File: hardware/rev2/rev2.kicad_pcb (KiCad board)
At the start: 2 copper layers, 24 parts, among them J1 Conn_01x09_Female, J2 RFM9X_header, J3 Conn_02x03_Odd_Even, U2 MPL3115A2, U3 Teensy3.6, U5 ADXL345BCCZ, U7 TPS2113ADRBR

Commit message: wip
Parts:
- moved VDD1 17.0 mm to (163.1, 131.8)
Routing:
- net 3.3V_TEENSY: track 9.55 -> 37.8 mm, vias 0 -> 2
- net Net-(C9-Pad1): track 11.3 -> 16.5 mm, vias 0 -> 1
- net GND: track 42.1 -> 46.1 mm, vias 4 -> 5
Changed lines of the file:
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@@
     (thickness 1.6)
     (drawings 18)
-    (tracks 147)
+    (tracks 172)
     (zones 0)
     (modules 24)
@@
   )
   (setup
-    (last_trace_width 0.55)
+    (last_trace_width 1)
     (user_trace_width 0.475)
     (user_trace_width 0.55)
@@
   )
   (module footprints:Test-Point-Pin_Drill2.79mm (layer F.Cu)
-    (at 178.943 137.795 180)
+    (at 163.068 131.7752 180)
     (fp_text reference VDD1 (at 0 3.98) (layer F.SilkS)
       (effects (font (size 1 1) (thickness 0.15)))
@@
   (segment (start 161.5821 113.8903) (end 157.6451 113.8903) (width 1) (layer F.Cu) (net 1) (status C00030))
   (segment (start 157.6451 113.8903) (end 153.7081 113.8903) (width 1) (layer F.Cu) (net 1) (status C00030))
-  (segment (start 163.6549 109.4179) (end 163.6549 111.0461) (width 1) (layer F.Cu) (net 1) (status 400010))
-  (segment (start 163.6395 113.8809) (end 163.6268 113.8936) (width 1) (layer B.Cu) (net 1))
-  (segment (start 163.6395 111.0615) (end 163.6395 113.8809) (width 1) (layer B.Cu) (net 1))
-  (via (at 163.6268 113.8936) (size 1.2) (drill 0.6) (layers F.Cu B.Cu) (net 1))
-  (segment (start 163.6108 113.8776) (end 163.6268 113.8936) (width 1) (layer F.Cu) (net 1))
-  (segment (start 163.6108 113.8776) (end 161.5821 113.8903) (width 1) (layer F.Cu) (net 1) (status 800010))
-  (via (at 163.6395 111.0615) (size 1.2) (drill 0.6) (layers F.Cu B.Cu) (net 1))
-  (segment (start 163.6549 111.0461) (end 163.6395 111.0615) (width 1) (layer F.Cu) (net 1))
   (segment (start 144.9545 110.5695) (end 144.78 110.744) (width 1) (layer F.Cu) (net 1))
   (segment (start 144.78 110.744) (end 144.9705 110.5535) (width 1) (layer F.Cu) (net 1))
@@
   (segment (start 150.622 108.8136) (end 151.5364 109.728) (width 1) (layer B.Cu) (net 1))
   (segment (start 151.5364 109.728) (end 151.5364 113.8936) (width 1) (layer B.Cu) (net 1))
-  (segment (start 161.5821 112.2553) (end 167.1701 112.2553) (width 0.25) (layer F.Cu) (net 2) (status 10))
-  (segment (start 169.5196 112.2553) (end 169.9006 112.6363) (width 0.25) (layer F.Cu) (net 2) (status C00030))
-  (segment (start 167.1701 112.2553) (end 169.5196 112.2553) (width 0.25) (layer F.Cu) (net 2) (status 800020))
+  (segment (start 139.7 110.76) (end 139.7 109.8804) (width 1) (layer F.Cu) (net 1) (status 400000))
+  (via (at 143.6116 108.9152) (size 0.8) (drill 0.4) (layers F.Cu B.Cu) (net 1))
+  (segment (start 142.1384 108.9152) (end 143.6116 108.9152) (width 1) (layer F.Cu) (net 1))
+  (via (at 142.1384 108.9152) (size 0.8) (drill 0.4) (layers F.Cu B.Cu) (net 1))
+  (segment (start 140.6652 108.9152) (end 142.1384 108.9152) (width 1) (layer B.Cu) (net 1))
+  (via (at 140.6652 108.9152) (size 0.8) (drill 0.4) (layers F.Cu B.Cu) (net 1))
+  (segment (start 139.7 109.8804) (end 140.6652 108.9152) (width 1) (layer F.Cu) (net 1))
+  (segment (start 163.6549 109.4179) (end 163.6549 111.8175) (width 0.55) (layer F.Cu) (net 1) (status 400000))
+  (segment (start 163.6549 111.8175) (end 161.5821 113.8903) (width 0.55) (layer F.Cu) (net 1) (status 800000))
   (segment (start 162.4049 109.4179) (end 162.4049 111.0675) (width 0.25) (layer F.Cu) (net 2) (status 400000))
   (segment (start 162.4049 111.0675) (end 161.5821 111.8903) (width 0.25) (layer F.Cu) (net 2) (status 800000))
+  (segment (start 161.5821 111.8903) (end 160.4993 111.8903) (width 0.25) (layer F.Cu) (net 2) (status 400000))
+  (segment (start 168.5417 113.9952) (end 169.9006 112.6363) (width 0.25) (layer B.Cu) (net 2) (status 800000))
+  (segment (start 160.528 113.9952) (end 168.5417 113.9952) (width 0.25) (layer B.Cu) (net 2))
+  (segment (start 159.8676 113.3348) (end 160.528 113.9952) (width 0.25) (layer B.Cu) (net 2))
+  (segment (start 159.8676 112.522) (end 159.8676 113.3348) (width 0.25) (layer B.Cu) (net 2))
+  (segment (start 160.4993 111.8903) (end 159.8676 112.522) (width 0.25) (layer F.Cu) (net 2))
+  (via (at 159.8676 112.522) (size 0.8) (drill 0.4) (layers F.Cu B.Cu) (net 2))
   (segment (start 135.763 87.376) (end 138.684 90.297) (width 0.25) (layer F.Cu) (net 3) (status 400000))
   (segment (start 157.353 101.6) (end 146.05 90.297) (width 0.25) (layer F.Cu) (net 3))
@@
   (segment (start 139.7 112.76) (end 142.875 112.76) (width 1) (layer F.Cu) (net 53) (status C00000))
   (segment (start 151.003 102.616) (end 151.003 104.8258) (width 1) (layer F.Cu) (net 53) (status 400000))
-  (segment (start 151.4958 107.503) (end 152.781 107.503) (width 0.55) (layer F.Cu) (net 53) (status 1800000))
-  (segment (start 151.003 107.0102) (end 151.4958 107.503) (width 0.55) (layer F.Cu) (net 53) (status 1000000))
-  (segment (start 151.003 104.8258) (end 151.003 107.0102) (width 0.55) (layer F.Cu) (net 53) (status 1000000))
+  (segment (start 151.4958 107.503) (end 152.781 107.503) (width 0.55) (layer F.Cu) (net 53) (status 800000))
+  (segment (start 151.003 107.0102) (end 151.4958 107.503) (width 0.55) (layer F.Cu) (net 53))
+  (segment (start 151.003 104.8258) (end 151.003 107.0102) (width 0.55) (layer F.Cu) (net 53))
+  (segment (start 147.0025 111.5475) (end 147.0025 112.8141) (width 0.55) (layer F.Cu) (net 53) (status 400000))
+  (segment (start 145.9925 112.8201) (end 145.9925 112.6303) (width 0.55) (layer F.Cu) (net 53))
+  (segment (start 145.9925 112.6303) (end 145.9925 111.5375) (width 0.55) (layer F.Cu) (net 53) (status 800000))
+  (segment (start 145.9992 112.8268) (end 145.9925 112.8201) (width 0.55) (layer F.Cu) (net 53))
+  (segment (start 146.9898 112.8268) (end 145.9992 112.8268) (width 0.55) (layer F.Cu) (net 53))
+  (segment (start 147.0025 112.8141) (end 146.9898 112.8268) (width 0.55) (layer F.Cu) (net 53))
+  (segment (start 145.9925 107.5375) (end 140.1633 107.5375) (width 0.55) (layer F.Cu) (net 53) (status 400000))
+  (segment (start 139.0236 112.76) (end 139.7 112.76) (width 0.55) (layer F.Cu) (net 53) (status 800000))
+  (segment (start 138.2776 112.014) (end 139.0236 112.76) (width 0.55) (layer F.Cu) (net 53))
+  (segment (start 138.2776 109.4232) (end 138.2776 112.014) (width 0.55) (layer F.Cu) (net 53))
+  (segment (start 140.1633 107.5375) (end 138.2776 109.4232) (width 0.55) (layer F.Cu) (net 53))
+  (segment (start 164.9049 109.4179) (end 164.9049 111.1585) (width 0.55) (layer F.Cu) (net 53) (status 400000))
+  (via (at 159.258 110.1344) (size 1.2) (drill 0.6) (layers F.Cu B.Cu) (net 53))
+  (segment (start 161.1884 112.0648) (end 159.258 110.1344) (width 0.55) (layer B.Cu) (net 53))
+  (segment (start 164.084 112.0648) (end 161.1884 112.0648) (width 0.55) (layer B.Cu) (net 53))
+  (segment (start 164.9476 111.2012) (end 164.084 112.0648) (width 0.55) (layer B.Cu) (net 53))
+  (via (at 164.9476 111.2012) (size 1.2) (drill 0.6) (layers F.Cu B.Cu) (net 53))
+  (segment (start 164.9049 111.1585) (end 164.9476 111.2012) (width 0.55) (layer F.Cu) (net 53))
+  (segment (start 142.875 112.76) (end 145.8628 112.76) (width 1) (layer F.Cu) (net 53) (status 400000))
+  (segment (start 145.8628 112.76) (end 145.9925 112.6303) (width 1) (layer F.Cu) (net 53) (status 1000000))
   (zone (net 53) (net_name 3.3V_TEENSY) (layer F.Cu) (hatch edge 0.508)
     (connect_pads (clearance 0.25))

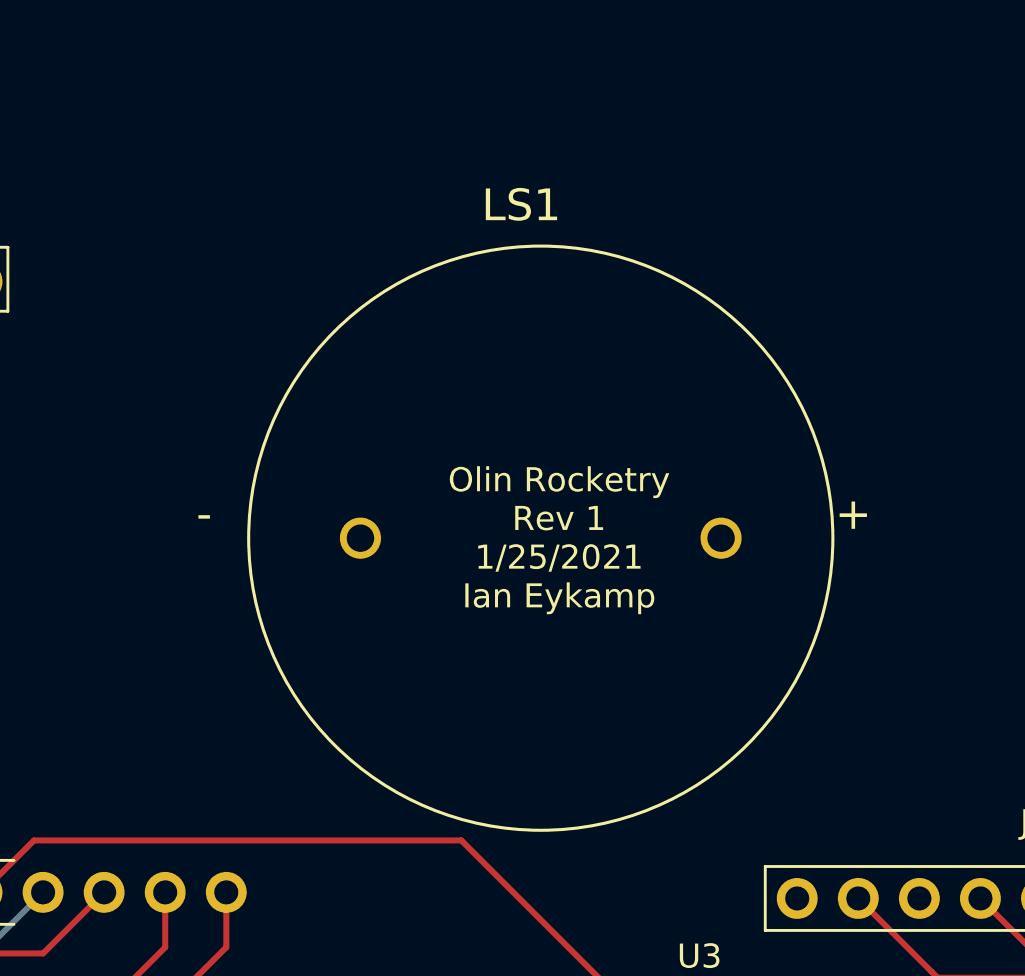
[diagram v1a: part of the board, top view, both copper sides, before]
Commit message: add debugging LEDs (may need to change)
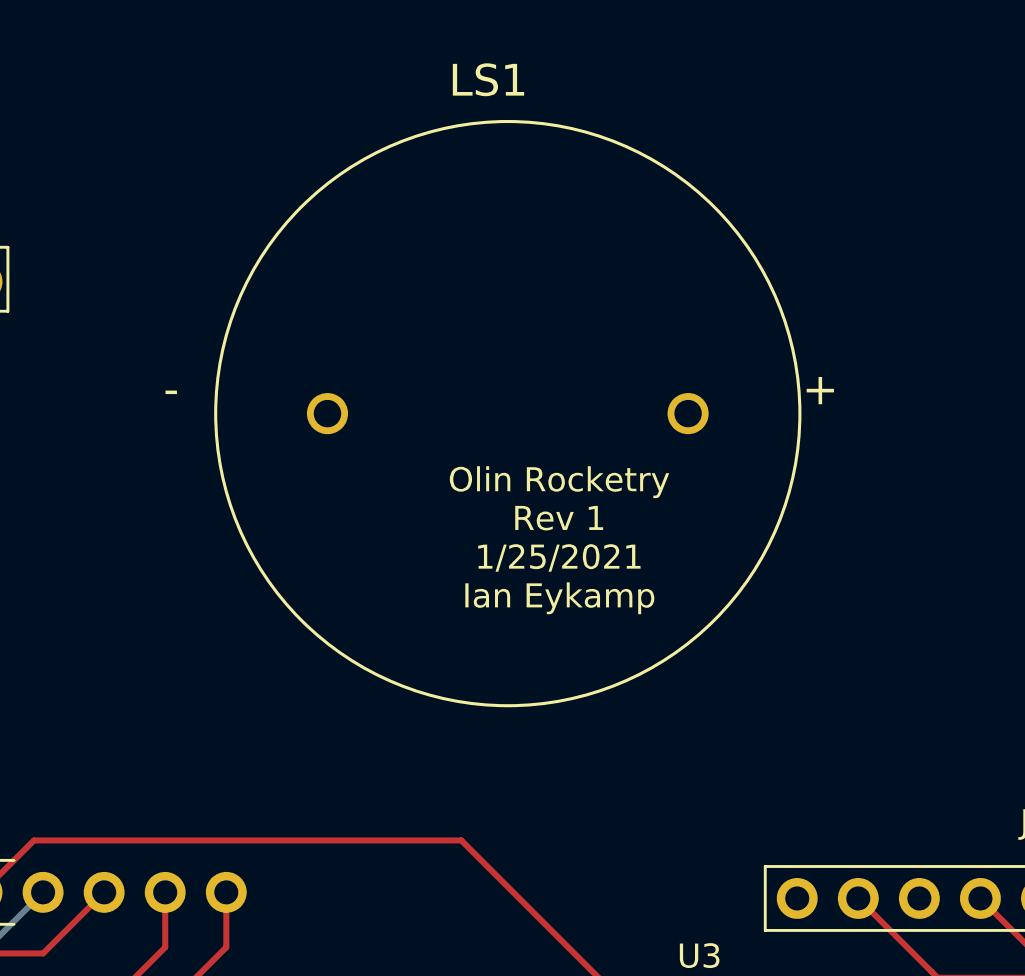
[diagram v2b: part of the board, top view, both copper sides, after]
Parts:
- moved LS1 5.36 mm to (140.4, 62.1)

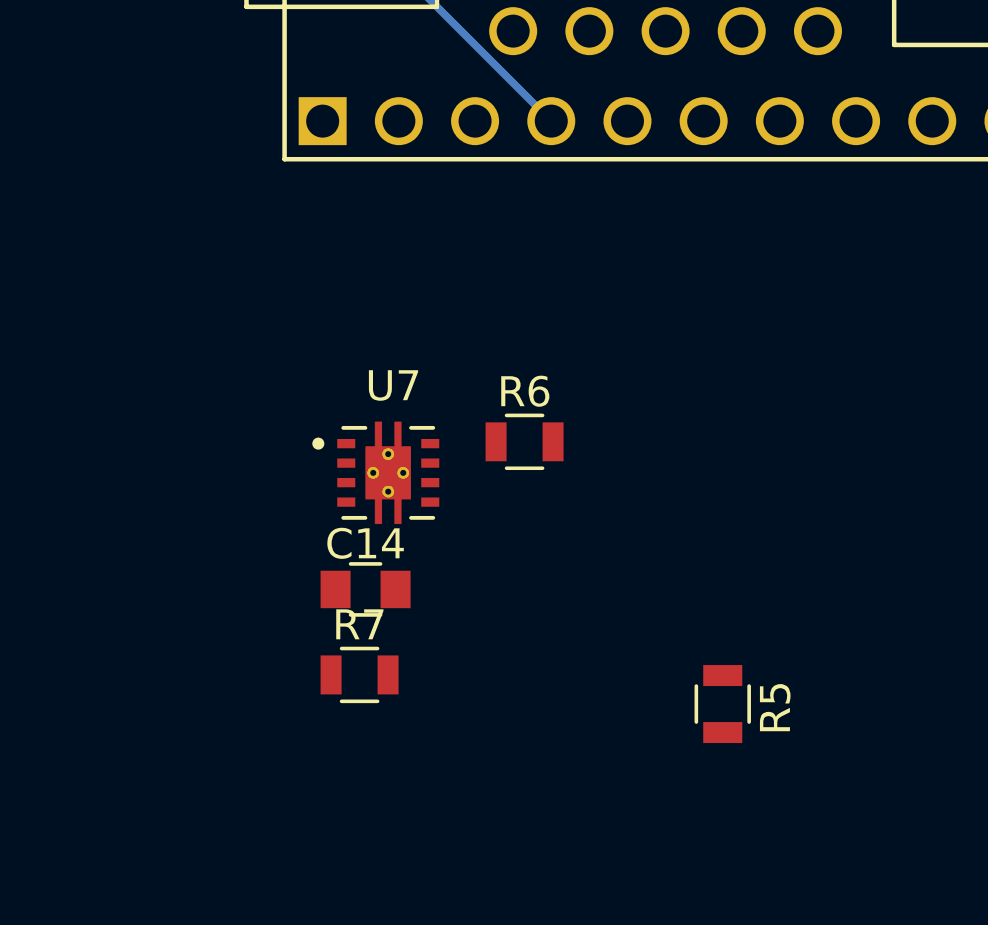
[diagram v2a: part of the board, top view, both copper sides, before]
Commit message: connect LEDs to Teensy, add ground connections
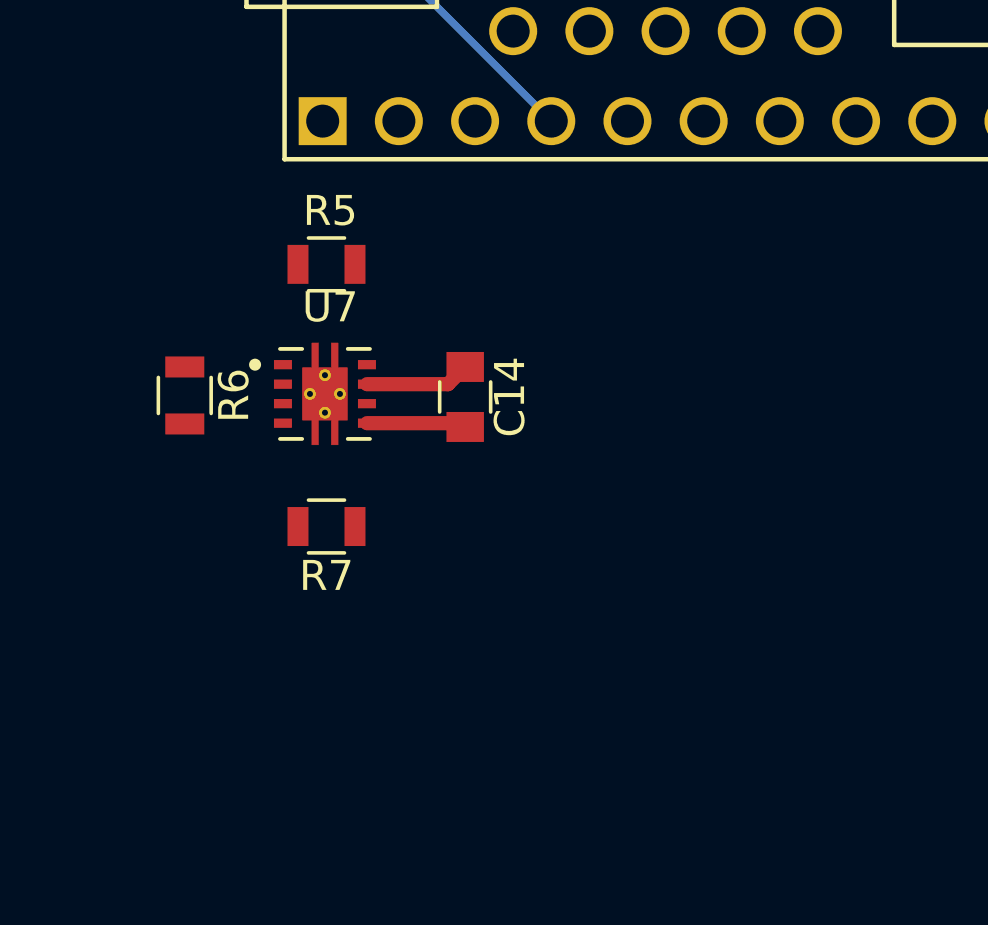
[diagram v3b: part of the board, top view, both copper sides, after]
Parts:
- moved R5 19.7 mm to (115.6, 107.4), turned to 0 degrees
- moved R6 11.4 mm to (110.8, 111.8), turned to 270 degrees
- moved C14 7.22 mm to (120.2, 111.8), turned to 270 degrees
- moved R7 5.07 mm to (115.6, 116.1), turned to 180 degrees
- moved U7 3.37 mm to (115.5, 111.7)
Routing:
- net BMS_to_Teensy: track 0.00 -> 3.51 mm
- net GND: track 46.1 -> 49.4 mm
